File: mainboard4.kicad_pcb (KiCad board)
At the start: 4 copper layers, 100 x 100 mm, 238 parts, among them J1 Conn_01x04_Pin, J10 RJMG201K21120FR, J11 690-019-298-412, J12 USB3_A, J13 USB_C_Receptacle_USB2.0_16P, J14 Micro_SD_Card_Det, J2 Conn_01x04_Pin, J3 Bus_M.2_Socket_B, J4 JST_SHBM04B-SRSS-TB, J5 THD-20-R, J6 Conn_02x07_Odd_Even, J7 Bus_M.2_Socket_E, J8 USB_A_Stacked, J9 Barrel_Jack, SW1 Right angle Tact button, SW2 SW_DIP_x04, SW3 SW_Push, U1 74LVC1G07SE-7, U10 MCP2562-E-SN, U11 MCP2562-E-SN, U12 STM32H723VGT6, U13 LAN8742A, U14 JMS578, U15 CAT250xxx, U16 LAN9514, U17 CAT250xxx, U18 RT9742SNGV, U2 BNO086, U3 RT9742GGJ5, U4 ASEK-32.768KHZ-L-R-T, U5 AP64502QSP-13, U6 ASEK-32.768KHZ-L-R-T, U7 AP64502, U8 AP22653W6, U9 CH221K, Y1 32.768khz, Y2 16Mhz, Y3 25Mhz, Y4 30Mhz, Y5 25Mhz

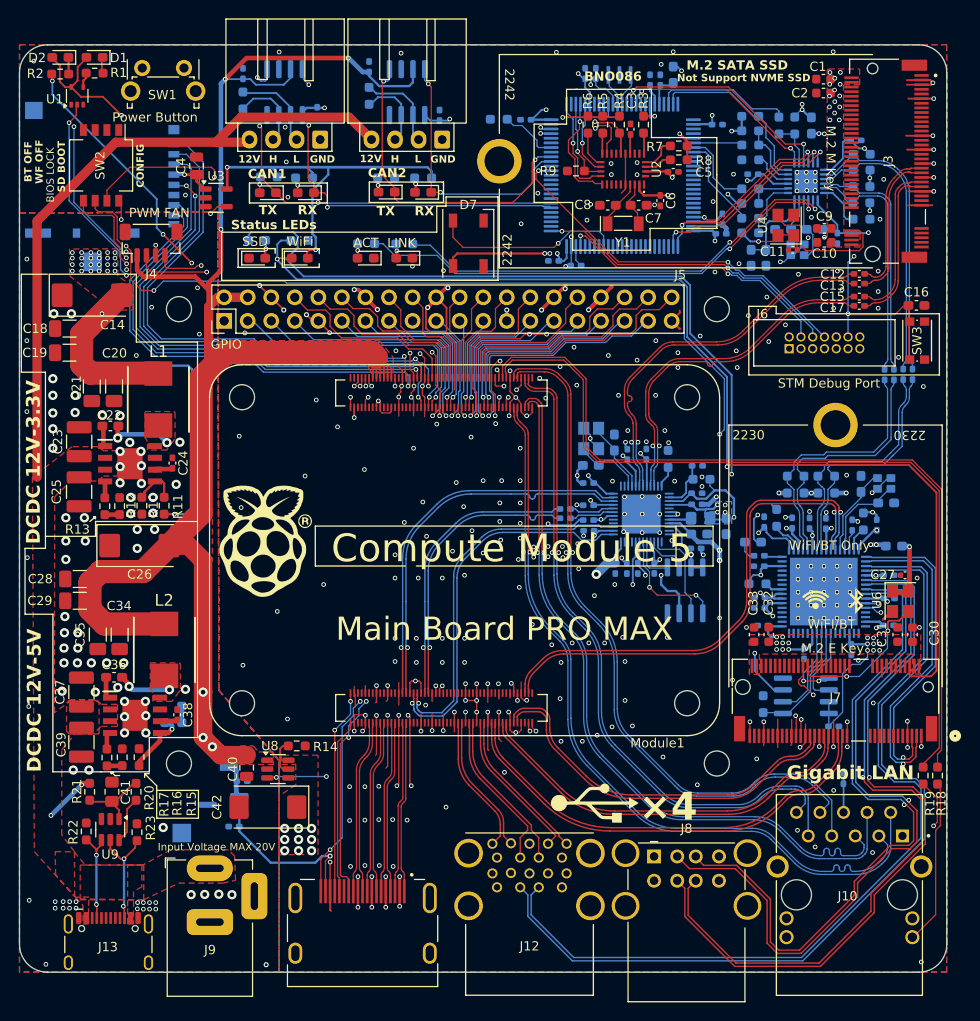
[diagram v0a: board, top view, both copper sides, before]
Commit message: add disable pin pullup
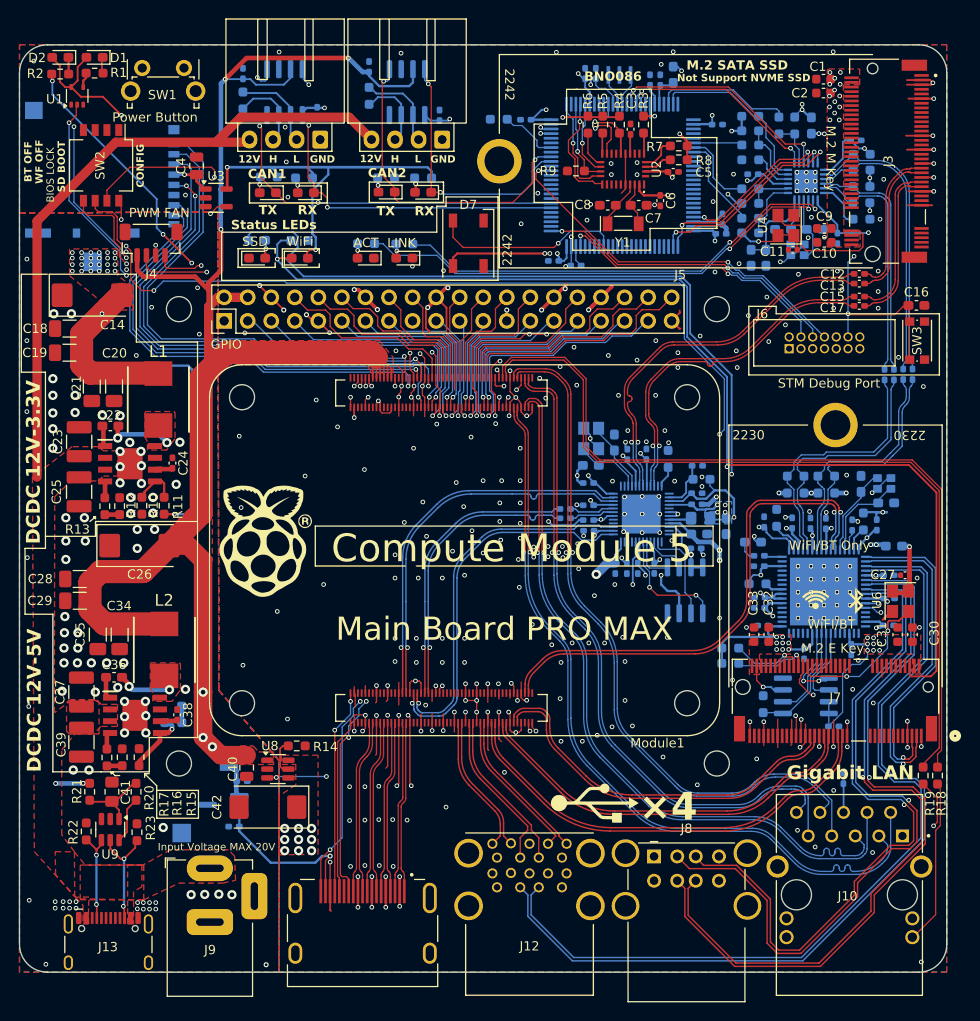
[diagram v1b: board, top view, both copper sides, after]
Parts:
- added R62: 100k, Resistor_SMD:R_0603_1608Metric_Pad0.98x0.95mm_HandSolder, B.Cu at (184.7, 100.0)
- added R63: 1k, Resistor_SMD:R_0603_1608Metric_Pad0.98x0.95mm_HandSolder, B.Cu at (184.7, 101.7)
- moved C84 0.10 mm to (193.3, 86.6)
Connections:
- J7 pad 54: unconnected-(J7-~{W_DISABLE2}-Pad54) -> Net-(J7-~{W_DISABLE2})
- J7 pad 56: unconnected-(J7-~{W_DISABLE1}-Pad56) -> Net-(J7-~{W_DISABLE1})
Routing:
- net Net-(J7-~{W_DISABLE2}): track 0.00 -> 8.07 mm, vias 0 -> 1
- net Net-(J7-~{W_DISABLE1}): track 0.00 -> 7.95 mm, vias 0 -> 1
- net +3.3V: track 307.4 -> 314.8 mm
- net +12V: track 78.2 -> 76.3 mm
- net GND: track 798.3 -> 800.2 mm, vias 410 -> 411
- net Net-(U13-LED1/REGOFF): track 52.8 -> 52.2 mm

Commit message: change design
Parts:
- moved R62 3.93 mm to (188.6, 100.5), turned to -90 degrees
- moved R63 2.55 mm to (186.9, 100.5), turned to -90 degrees
- moved J8 0.52 mm to (176.5, 122.0)
- moved R59 0.10 mm to (188.2, 106.2)
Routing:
- net +3.3V: track 314.8 -> 308.9 mm
- net Net-(J7-~{W_DISABLE1}): track 7.95 -> 4.16 mm
- net /USB2Ethernet/USB5DP: track 74.0 -> 77.8 mm
- net /USB2Ethernet/VDDA: track 39.6 -> 42.1 mm, vias 12 -> 11
- net Net-(D10-K): track 118.8 -> 117.1 mm
- net /USB2Ethernet/USB4DP: track 77.7 -> 79.4 mm
- net /USB2DP: track 92.8 -> 94.5 mm
- net /USB2SATA/HDD_LED: track 101.1 -> 100.0 mm
- net Net-(J7-~{W_DISABLE2}): track 8.07 -> 7.38 mm
- net /VBUS: track 88.9 -> 89.6 mm
- net /USB2Ethernet/USB5DN: track 77.3 -> 77.9 mm
- net /CM5_PCIe/USB_D-: track 34.8 -> 35.4 mm
- net GND: track 800.2 -> 800.1 mm, vias 411 -> 412
- added copper zone on B.Cu, net +3.3V
